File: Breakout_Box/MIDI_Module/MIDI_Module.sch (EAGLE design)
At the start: 71 parts, among them T1 2N2222, T2 2N2222, U1 LMV324, U2 LMV324, U3 MIC5205-5.0YM5-TR, U4 MIC5205-3.3YM5-TR

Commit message: Licenses
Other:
- note added: "MIDI Module for Nexus Project by Cycfi Research is licensed under a Creative Commons Attribution-ShareAlike 4.0 International License. Copyright CYCFI Research Inc. 2013-2016"
- note removed: "Nexus Project by Cycfi Research is licensed under a Creative Commons Attribution-NonCommercial 4.0 International License. http://creativecommons.org/licenses/by-nc/4.0/ Copyright CYCFI Research Inc. 2013-2016"
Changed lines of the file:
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@@
 <grid distance="0.1" unitdist="inch" unit="inch" style="lines" multiple="1" display="no" altdistance="0.01" altunitdist="inch" altunit="inch"/>
 <layers>
-<layer number="1" name="Top" color="4" fill="1" visible="yes" active="no"/>
-<layer number="2" name="Route2" color="1" fill="3" visible="yes" active="no"/>
-<layer number="3" name="Route3" color="4" fill="3" visible="yes" active="no"/>
-<layer number="4" name="Route4" color="1" fill="4" visible="yes" active="no"/>
-<layer number="5" name="Route5" color="4" fill="4" visible="yes" active="no"/>
-<layer number="6" name="Route6" color="1" fill="8" visible="yes" active="no"/>
-<layer number="7" name="Route7" color="4" fill="8" visible="yes" active="no"/>
-<layer number="8" name="Route8" color="1" fill="2" visible="yes" active="no"/>
-<layer number="9" name="Route9" color="4" fill="2" visible="yes" active="no"/>
-<layer number="10" name="Route10" color="1" fill="7" visible="yes" active="no"/>
-<layer number="11" name="Route11" color="4" fill="7" visible="yes" active="no"/>
-<layer number="12" name="Route12" color="1" fill="5" visible="yes" active="no"/>
-<layer number="13" name="Route13" color="4" fill="5" visible="yes" active="no"/>
-<layer number="14" name="Route14" color="1" fill="6" visible="yes" active="no"/>
-<layer number="15" name="Route15" color="4" fill="6" visible="yes" active="no"/>
-<layer number="16" name="Bottom" color="1" fill="1" visible="yes" active="no"/>
-<layer number="17" name="Pads" color="2" fill="1" visible="yes" active="no"/>
-<layer number="18" name="Vias" color="2" fill="1" visible="yes" active="no"/>
-<layer number="19" name="Unrouted" color="6" fill="1" visible="yes" active="no"/>
-<layer number="20" name="Dimension" color="15" fill="1" visible="yes" active="no"/>
-<layer number="21" name="tPlace" color="7" fill="1" visible="yes" active="no"/>
-<layer number="22" name="bPlace" color="7" fill="1" visible="yes" active="no"/>
-<layer number="23" name="tOrigins" color="15" fill="1" visible="yes" active="no"/>
-<layer number="24" name="bOrigins" color="15" fill="1" visible="yes" active="no"/>
-<layer number="25" name="tNames" color="7" fill="1" visible="yes" active="no"/>
-<layer number="26" name="bNames" color="7" fill="1" visible="yes" active="no"/>
-<layer number="27" name="tValues" color="7" fill="1" visible="yes" active="no"/>
-<layer number="28" name="bValues" color="7" fill="1" visible="yes" active="no"/>
+<layer number="1" name="Top" color="4" fill="1" visible="no" active="no"/>
+<layer number="2" name="Route2" color="1" fill="3" visible="no" active="no"/>
+<layer number="3" name="Route3" color="4" fill="3" visible="no" active="no"/>
+<layer number="4" name="Route4" color="1" fill="4" visible="no" active="no"/>
+<layer number="5" name="Route5" color="4" fill="4" visible="no" active="no"/>
+<layer number="6" name="Route6" color="1" fill="8" visible="no" active="no"/>
+<layer number="7" name="Route7" color="4" fill="8" visible="no" active="no"/>
+<layer number="8" name="Route8" color="1" fill="2" visible="no" active="no"/>
+<layer number="9" name="Route9" color="4" fill="2" visible="no" active="no"/>
+<layer number="10" name="Route10" color="1" fill="7" visible="no" active="no"/>
+<layer number="11" name="Route11" color="4" fill="7" visible="no" active="no"/>
+<layer number="12" name="Route12" color="1" fill="5" visible="no" active="no"/>
+<layer number="13" name="Route13" color="4" fill="5" visible="no" active="no"/>
+<layer number="14" name="Route14" color="1" fill="6" visible="no" active="no"/>
+<layer number="15" name="Route15" color="4" fill="6" visible="no" active="no"/>
+<layer number="16" name="Bottom" color="1" fill="1" visible="no" active="no"/>
+<layer number="17" name="Pads" color="2" fill="1" visible="no" active="no"/>
+<layer number="18" name="Vias" color="2" fill="1" visible="no" active="no"/>
+<layer number="19" name="Unrouted" color="6" fill="1" visible="no" active="no"/>
+<layer number="20" name="Dimension" color="15" fill="1" visible="no" active="no"/>
+<layer number="21" name="tPlace" color="7" fill="1" visible="no" active="no"/>
+<layer number="22" name="bPlace" color="7" fill="1" visible="no" active="no"/>
+<layer number="23" name="tOrigins" color="15" fill="1" visible="no" active="no"/>
+<layer number="24" name="bOrigins" color="15" fill="1" visible="no" active="no"/>
+<layer number="25" name="tNames" color="7" fill="1" visible="no" active="no"/>
+<layer number="26" name="bNames" color="7" fill="1" visible="no" active="no"/>
+<layer number="27" name="tValues" color="7" fill="1" visible="no" active="no"/>
+<layer number="28" name="bValues" color="7" fill="1" visible="no" active="no"/>
 <layer number="29" name="tStop" color="7" fill="3" visible="no" active="no"/>
 <layer number="30" name="bStop" color="7" fill="6" visible="no" active="no"/>
@@
 <layer number="35" name="tGlue" color="7" fill="4" visible="no" active="no"/>
 <layer number="36" name="bGlue" color="7" fill="5" visible="no" active="no"/>
-<layer number="37" name="tTest" color="7" fill="1" visible="yes" active="no"/>
-<layer number="38" name="bTest" color="7" fill="1" visible="yes" active="no"/>
+<layer number="37" name="tTest" color="7" fill="1" visible="no" active="no"/>
+<layer number="38" name="bTest" color="7" fill="1" visible="no" active="no"/>
 <layer number="39" name="tKeepout" color="4" fill="11" visible="no" active="no"/>
 <layer number="40" name="bKeepout" color="1" fill="11" visible="no" active="no"/>
@@
 <layer number="44" name="Drills" color="7" fill="1" visible="no" active="no"/>
 <layer number="45" name="Holes" color="7" fill="1" visible="no" active="no"/>
-<layer number="46" name="Milling" color="3" fill="1" visible="yes" active="no"/>
-<layer number="47" name="Measures" color="7" fill="1" visible="yes" active="no"/>
-<layer number="48" name="Document" color="7" fill="1" visible="yes" active="no"/>
-<layer number="49" name="Reference" color="7" fill="1" visible="yes" active="no"/>
-<layer number="50" name="dxf" color="7" fill="1" visible="yes" active="no"/>
-<layer number="51" name="tDocu" color="7" fill="1" visible="yes" active="no"/>
-<layer number="52" name="bDocu" color="7" fill="1" visible="yes" active="no"/>
-<layer number="53" name="tGND_GNDA" color="7" fill="9" visible="yes" active="no"/>
-<layer number="54" name="bGND_GNDA" color="1" fill="9" visible="yes" active="no"/>
-<layer number="56" name="wert" color="7" fill="1" visible="yes" active="no"/>
-<layer number="57" name="tCAD" color="7" fill="1" visible="yes" active="no"/>
-<layer number="59" name="tCarbon" color="7" fill="1" visible="yes" active="no"/>
-<layer number="60" name="bCarbon" color="7" fill="1" visible="yes" active="no"/>
+<layer number="46" name="Milling" color="3" fill="1" visible="no" active="no"/>
+<layer number="47" name="Measures" color="7" fill="1" visible="no" active="no"/>
+<layer number="48" name="Document" color="7" fill="1" visible="no" active="no"/>
+<layer number="49" name="Reference" color="7" fill="1" visible="no" active="no"/>
+<layer number="50" name="dxf" color="7" fill="1" visible="no" active="no"/>
+<layer number="51" name="tDocu" color="7" fill="1" visible="no" active="no"/>
+<layer number="52" name="bDocu" color="7" fill="1" visible="no" active="no"/>
+<layer number="53" name="tGND_GNDA" color="7" fill="9" visible="no" active="no"/>
+<layer number="54" name="bGND_GNDA" color="1" fill="9" visible="no" active="no"/>
+<layer number="56" name="wert" color="7" fill="1" visible="no" active="no"/>
+<layer number="57" name="tCAD" color="7" fill="1" visible="no" active="no"/>
+<layer number="59" name="tCarbon" color="7" fill="1" visible="no" active="no"/>
+<layer number="60" name="bCarbon" color="7" fill="1" visible="no" active="no"/>
 <layer number="90" name="Modules" color="5" fill="1" visible="yes" active="yes"/>
 <layer number="91" name="Nets" color="2" fill="1" visible="yes" active="yes"/>
@@
 <text x="30.48" y="93.98" size="1.778" layer="95">DGND</text>
 <text x="30.48" y="96.52" size="1.778" layer="95">DGND</text>
-<text x="19.05" y="12.7" size="2.54" layer="95">Nexus Project by Cycfi Research is licensed under a
-Creative Commons Attribution-NonCommercial 4.0
-International License.
-http://creativecommons.org/licenses/by-nc/4.0/
+<text x="11.43" y="10.16" size="2.54" layer="95">MIDI Module for Nexus Project by Cycfi Research is licensed under a
+Creative Commons Attribution-ShareAlike 4.0 International License.
 Copyright CYCFI Research Inc. 2013-2016</text>
 </plain>
@@
 <wire x1="230.505" y1="96.52" x2="231.775" y2="96.52" width="0.1524" layer="94"/>
 <wire x1="214.63" y1="180.34" x2="214.63" y2="35.56" width="0.1524" layer="94" style="longdash"/>
-<text x="12.7" y="5.08" size="2.54" layer="95">Nexus Project by Cycfi Research is licensed under a
-Creative Commons Attribution-NonCommercial 4.0
-International License.
-http://creativecommons.org/licenses/by-nc/4.0/
+<text x="12.7" y="5.08" size="2.54" layer="95">MIDI Module for Nexus Project by Cycfi Research is licensed under a
+Creative Commons Attribution-ShareAlike 4.0 International License.
 Copyright CYCFI Research Inc. 2013-2016</text>
 </plain>
@@
 <wire x1="86.36" y1="142.875" x2="101.6" y2="142.875" width="0.2032" layer="95"/>
 <wire x1="101.6" y1="142.875" x2="103.505" y2="144.78" width="0.2032" layer="95"/>
-<text x="20.32" y="8.89" size="2.54" layer="95">Nexus Project by Cycfi Research is licensed under a
-Creative Commons Attribution-NonCommercial 4.0
-International License.
-http://creativecommons.org/licenses/by-nc/4.0/
+<text x="12.7" y="16.51" size="2.54" layer="95">MIDI Module for Nexus Project by Cycfi Research is licensed under a
+Creative Commons Attribution-ShareAlike 4.0 International License.
 Copyright CYCFI Research Inc. 2013-2016</text>
 </plain>

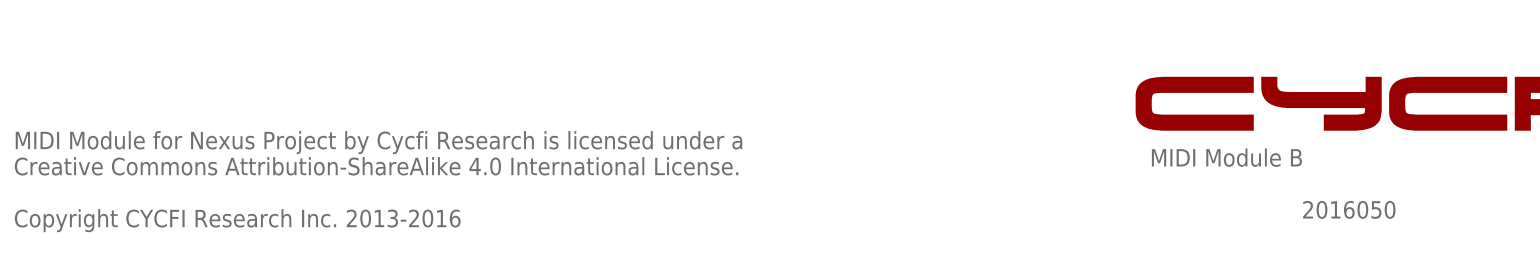
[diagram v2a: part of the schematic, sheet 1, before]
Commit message: Updated copyright and document number of schematics
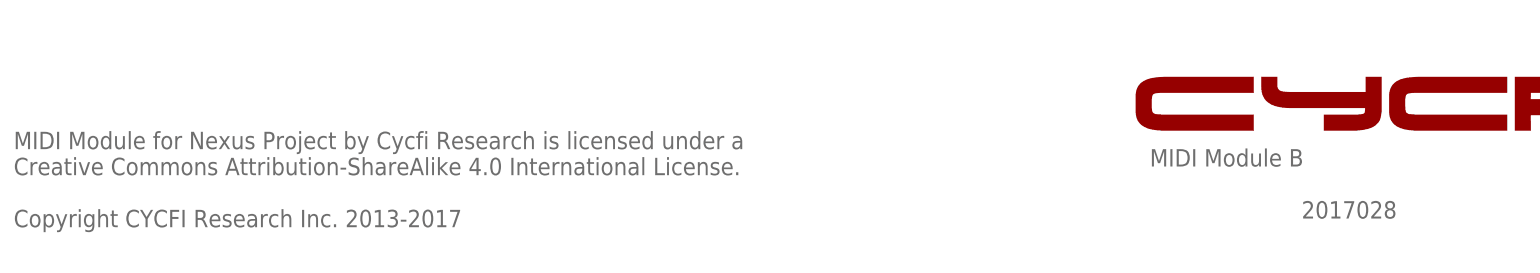
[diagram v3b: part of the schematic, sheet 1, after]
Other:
- note added: "2017028"
- note added: "MIDI Module for Nexus Project by Cycfi Research is licensed under a Creative Commons Attribution-ShareAlike 4.0 International License. Copyright CYCFI Research Inc. 2013-2017"
- note removed: "2016050"
- note removed: "MIDI Module for Nexus Project by Cycfi Research is licensed under a Creative Commons Attribution-ShareAlike 4.0 International License. Copyright CYCFI Research Inc. 2013-2016"
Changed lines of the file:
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@@
 <?xml version="1.0" encoding="utf-8"?>
 <!DOCTYPE eagle SYSTEM "eagle.dtd">
-<eagle version="6.3">
+<eagle version="7.6.0">
 <drawing>
 <settings>
@@
 <text x="177.8" y="19.05" size="2.54" layer="95">MIDI Module B</text>
 <text x="252.73" y="6.985" size="2.54" layer="95">v0.9</text>
-<text x="200.025" y="11.43" size="2.54" layer="95">2016050</text>
+<text x="200.025" y="11.43" size="2.54" layer="95">2017028</text>
 <wire x1="150.8125" y1="82.8675" x2="150.8125" y2="79.6925" width="0.254" layer="95"/>
 <wire x1="150.8125" y1="79.6925" x2="163.5125" y2="79.6925" width="0.254" layer="95"/>
@@
 <text x="11.43" y="10.16" size="2.54" layer="95">MIDI Module for Nexus Project by Cycfi Research is licensed under a
 Creative Commons Attribution-ShareAlike 4.0 International License.
-Copyright CYCFI Research Inc. 2013-2016</text>
+Copyright CYCFI Research Inc. 2013-2017</text>
 <rectangle x1="179.80469375" y1="24.29065625" x2="193.0330125" y2="24.29954375" layer="94"/>
 <rectangle x1="203.283184375" y1="24.29065625" x2="207.683734375" y2="24.29954375" layer="94"/>
@@
 <text x="177.8" y="19.05" size="2.54" layer="95">MIDI Module A</text>
 <text x="252.73" y="6.985" size="2.54" layer="95">v0.9</text>
-<text x="200.025" y="11.43" size="2.54" layer="95">2016050</text>
+<text x="200.025" y="11.43" size="2.54" layer="95">2017028</text>
 <text x="142.24" y="122.555" size="1.778" layer="95" rot="MR0">P3.3</text>
 <text x="142.24" y="120.015" size="1.778" layer="95" rot="MR0">P3.2</text>
@@
 <text x="12.7" y="5.08" size="2.54" layer="95">MIDI Module for Nexus Project by Cycfi Research is licensed under a
 Creative Commons Attribution-ShareAlike 4.0 International License.
-Copyright CYCFI Research Inc. 2013-2016</text>
+Copyright CYCFI Research Inc. 2013-2017</text>
 <rectangle x1="179.80469375" y1="24.29065625" x2="193.0330125" y2="24.29954375" layer="94"/>
 <rectangle x1="203.283184375" y1="24.29065625" x2="207.683734375" y2="24.29954375" layer="94"/>
@@
 <wire x1="161.925" y1="143.51" x2="174.3075" y2="143.51" width="0.254" layer="95"/>
 <wire x1="174.3075" y1="143.51" x2="175.895" y2="145.0975" width="0.254" layer="95"/>
-<text x="200.025" y="11.43" size="2.54" layer="95">2016050</text>
+<text x="200.025" y="11.43" size="2.54" layer="95">2017028</text>
 <wire x1="172.085" y1="101.2825" x2="170.4975" y2="102.87" width="0.254" layer="95"/>
 <wire x1="170.4975" y1="102.87" x2="161.925" y2="102.87" width="0.254" layer="95"/>
@@
 <text x="12.7" y="16.51" size="2.54" layer="95">MIDI Module for Nexus Project by Cycfi Research is licensed under a
 Creative Commons Attribution-ShareAlike 4.0 International License.
-Copyright CYCFI Research Inc. 2013-2016</text>
+Copyright CYCFI Research Inc. 2013-2017</text>
 <rectangle x1="179.80469375" y1="24.29065625" x2="193.0330125" y2="24.29954375" layer="94"/>
 <rectangle x1="203.283184375" y1="24.29065625" x2="207.683734375" y2="24.29954375" layer="94"/>

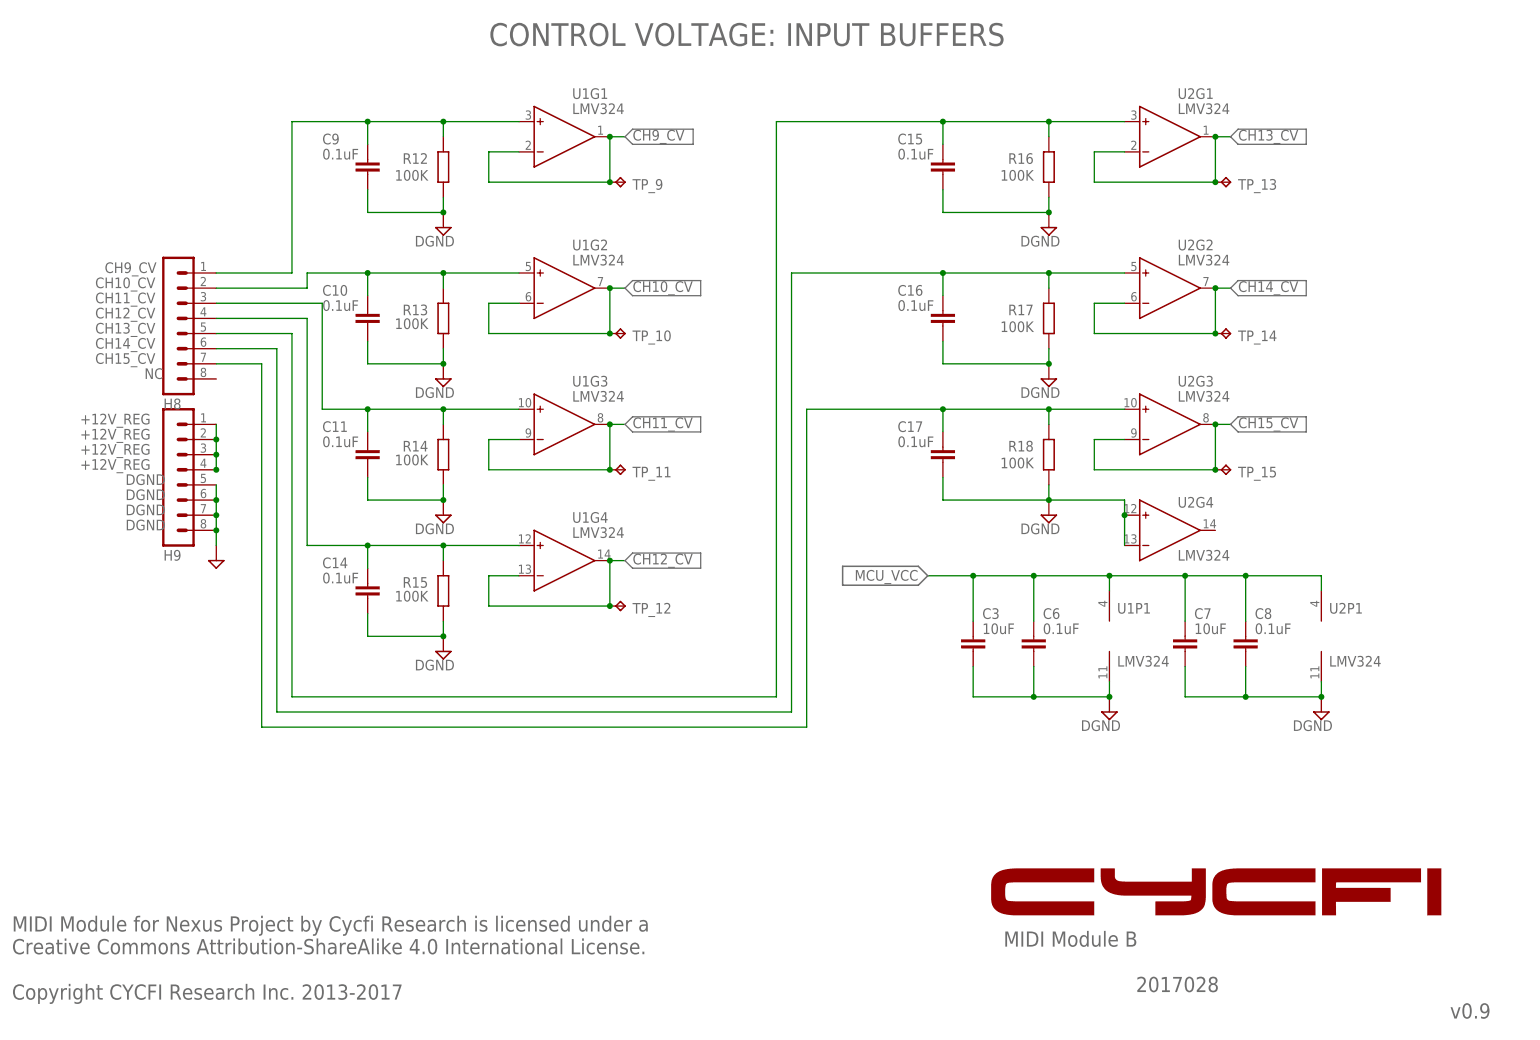
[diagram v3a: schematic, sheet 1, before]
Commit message: Create version_2.0 with updated main and midi modules
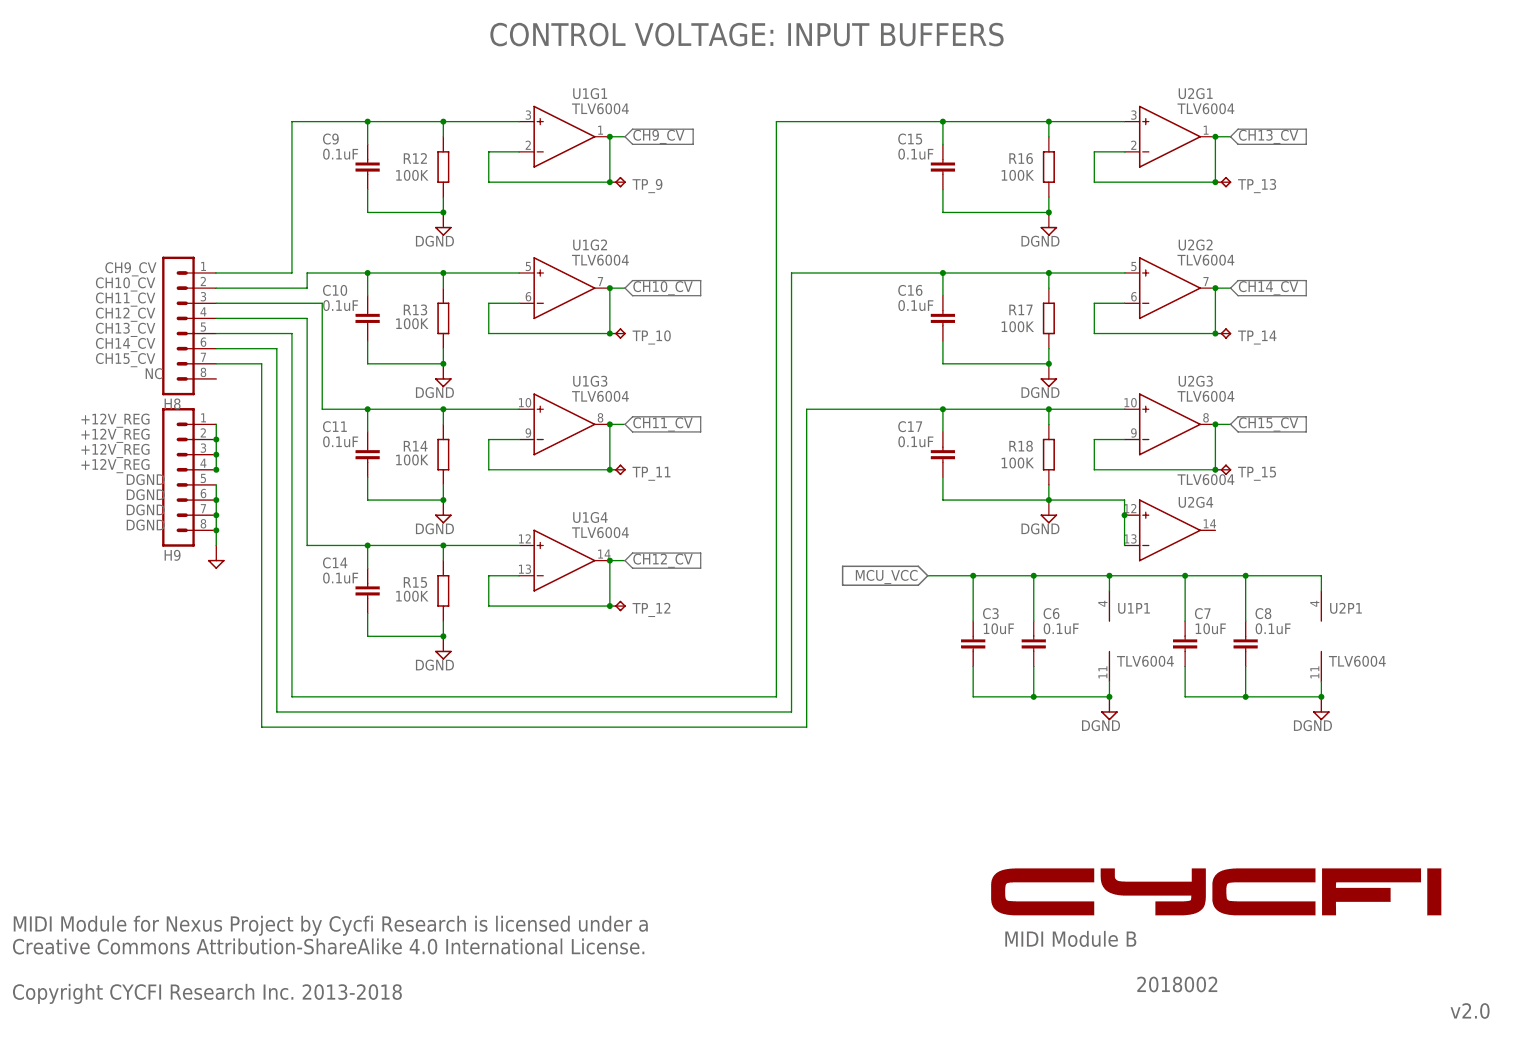
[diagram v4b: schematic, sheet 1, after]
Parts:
- U1, U2: value LMV324 -> TLV6004; device CYCFI_semicon:LMV324 -> CYCFI_semicon:TLV6004
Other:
- note added: "2018002"
- note added: "MIDI Module for Nexus Project by Cycfi Research is licensed under a Creative Commons Attribution-ShareAlike 4.0 International License. Copyright CYCFI Research Inc. 2013-2018"
- note added: "v2.0"
- note removed: "2017028"
- note removed: "MIDI Module for Nexus Project by Cycfi Research is licensed under a Creative Commons Attribution-ShareAlike 4.0 International License. Copyright CYCFI Research Inc. 2013-2017"
- note removed: "v0.9"
- note removed: "v0.92"
